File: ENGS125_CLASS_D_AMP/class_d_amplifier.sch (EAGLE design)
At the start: 24 parts, among them J1 BANANA_JACK_CT3151, J2 BANANA_JACK_CT3151, J3 BANANA_JACK_CT3151, J4 BANANA_JACK_CT3151, J5 BANANA_JACK_CT3151, J6 BANANA_JACK_CT3151, M1 BSC050NE2LSATMA1, M2 BSC050NE2LSATMA1, U1 LTC6992TSOT-23, U2 LTC4449

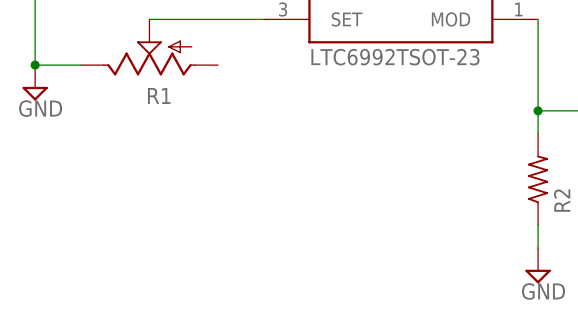
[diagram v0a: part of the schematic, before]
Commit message: Added Thayer shield to silkscreen on layout
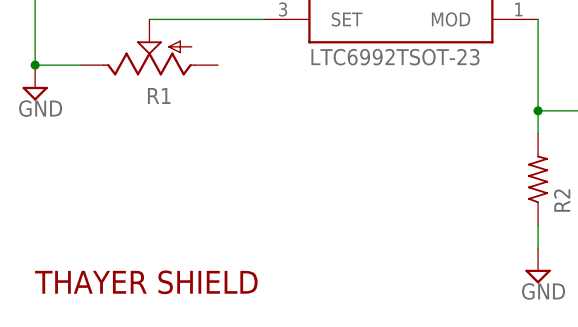
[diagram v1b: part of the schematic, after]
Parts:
- added U$1: THAYER, Engs125_lib_UPDATEFeb22_with_logo:THAYER
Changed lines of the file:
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@@
 <part name="J6" library="Engs125_lib_UPDATEFeb22" deviceset="BANANA_JACK_CT3151" device=""/>
 <part name="C8" library="Engs125_library" deviceset="C-US" device="" value="0.1u"/>
+<part name="U$1" library="Engs125_lib_UPDATEFeb22_with_logo" deviceset="THAYER" device=""/>
 </parts>
 <sheets>
@@
 <attribute name="VALUE" x="188.976" y="66.929" size="1.778" layer="96"/>
 </instance>
+<instance part="U$1" gate="G$1" x="-20.32" y="15.24" smashed="yes"/>
 </instances>
 <busses>

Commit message: Implemented edits from discussion with Stauth: GND pins, Gate pins, and extra input cap.
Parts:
- added C9: 1uF, Engs125_library:C-US
- added JP3, JP4, JP5, JP6, JP7: (no value), Engs125_lib_UPDATEFeb22:PINHD-1X1
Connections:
- net BG: now also JP4.1
- net GND: now also C9.2, JP5.1, JP6.1, JP7.1
- net TG: now also JP3.1
- net VIN: now also C9.1
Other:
- note added: "BG Probe"
- note added: "TG Probe"
- moved on the sheet: C5, C7

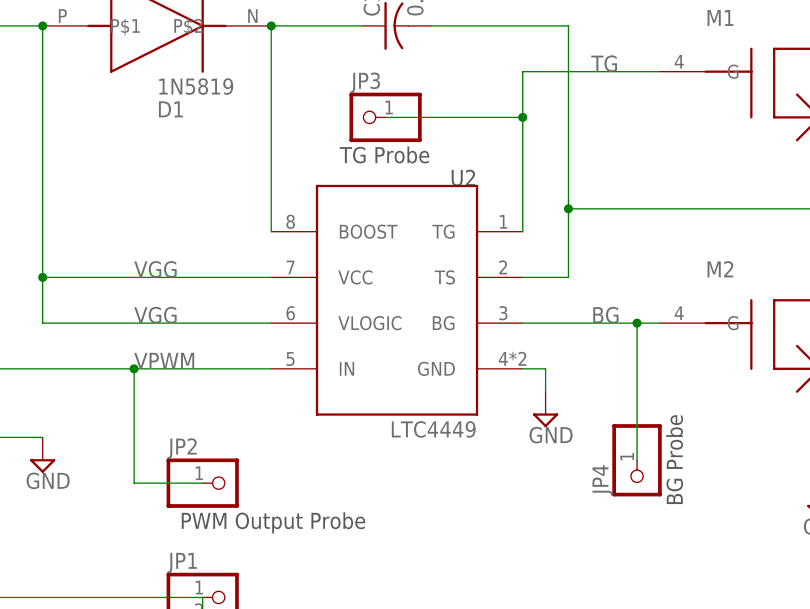
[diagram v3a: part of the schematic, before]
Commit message: Replaced gate driver IC with LTC4442
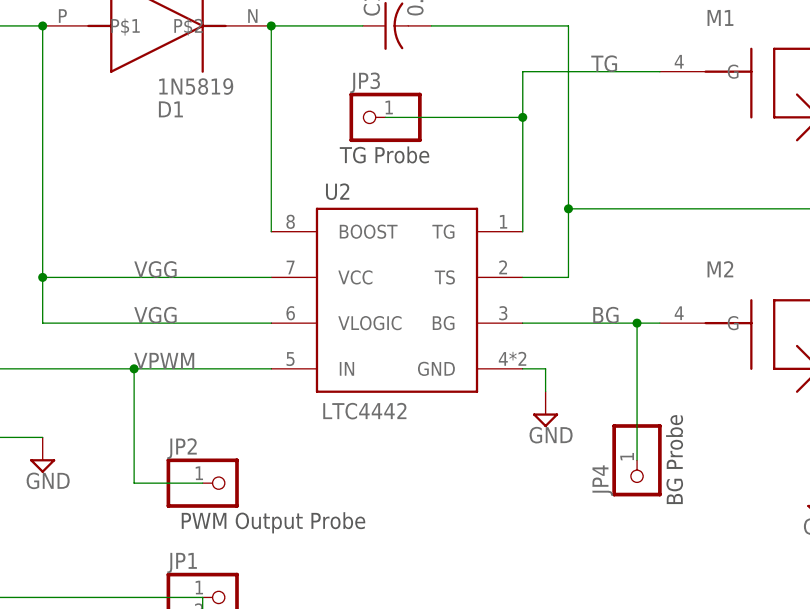
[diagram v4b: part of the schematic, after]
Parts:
- U2: value LTC4449 -> LTC4442; device Engs125_library:LTC4449 -> Engs125_lib_NEW_UPDATE_USE_THIS:LTC4442
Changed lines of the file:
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@@
 </classes>
 <parts>
-<part name="U2" library="Engs125_library" deviceset="LTC4449" device=""/>
+<part name="U2" library="Engs125_lib_NEW_UPDATE_USE_THIS" deviceset="LTC4442" device="" value="LTC4442"/>
 <part name="SUPPLY1" library="Engs125_library" deviceset="GND" device=""/>
 <part name="C3" library="Engs125_library" deviceset="C-US" device="" value="1uF"/>
@@
 </plain>
 <instances>
-<instance part="U2" gate="G$1" x="81.28" y="68.58" smashed="yes" rot="MR0">
-<attribute name="NAME" x="91.44" y="81.28" size="1.778" layer="97" rot="MR0"/>
-<attribute name="VALUE" x="91.44" y="53.34" size="1.778" layer="96" rot="MR0"/>
+<instance part="U2" gate="G$1" x="83.82" y="71.12" smashed="yes" rot="MR0">
+<attribute name="NAME" x="77.47" y="79.756" size="1.778" layer="97" rot="MR0"/>
+<attribute name="VALUE" x="83.82" y="55.372" size="1.778" layer="96" rot="MR0"/>
 </instance>
 <instance part="SUPPLY1" gate="GND" x="-20.32" y="38.1" smashed="yes">

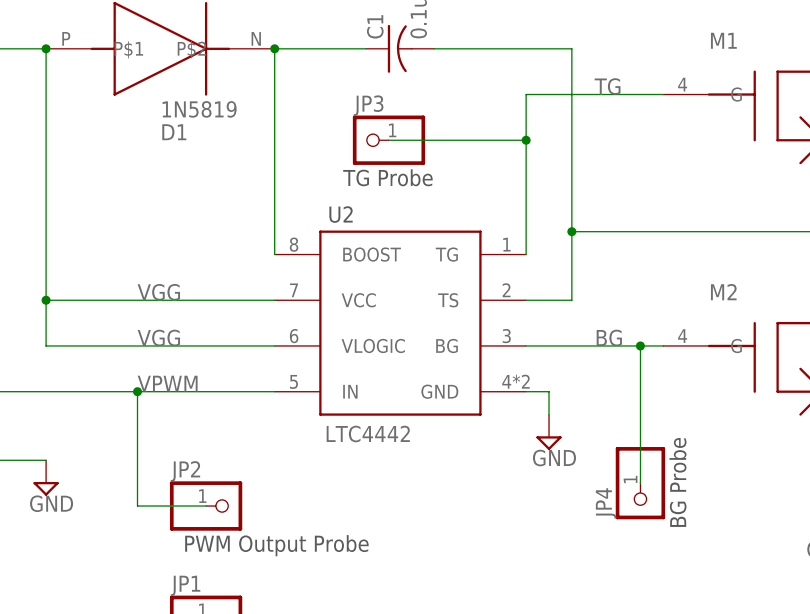
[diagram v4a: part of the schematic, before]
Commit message: Added converter specs to silkscreen
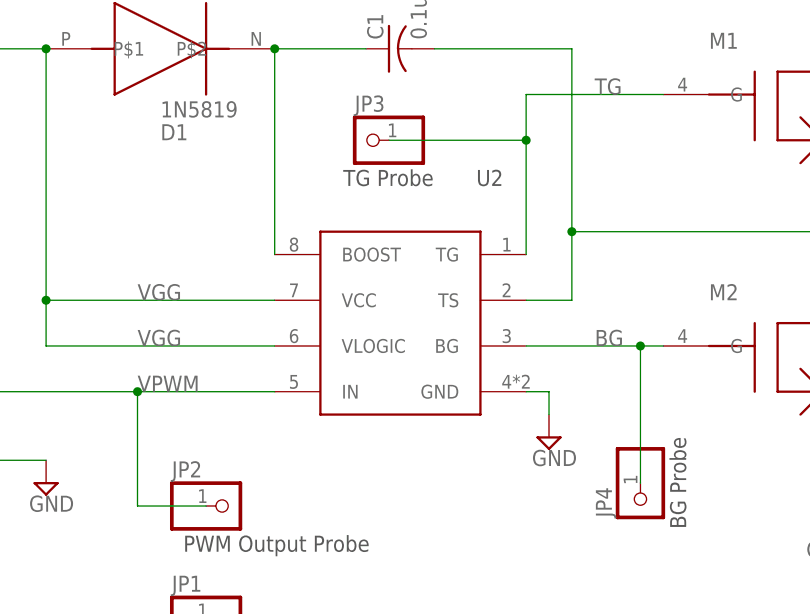
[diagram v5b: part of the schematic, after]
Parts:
- U2: value LTC4442 -> (none)
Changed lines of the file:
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@@
 </classes>
 <parts>
-<part name="U2" library="Engs125_lib_NEW_UPDATE_USE_THIS" deviceset="LTC4442" device="" value="LTC4442"/>
+<part name="U2" library="Engs125_lib_NEW_UPDATE_USE_THIS" deviceset="LTC4442" device=""/>
 <part name="SUPPLY1" library="Engs125_library" deviceset="GND" device=""/>
 <part name="C3" library="Engs125_library" deviceset="C-US" device="" value="1uF"/>
@@
 <instances>
 <instance part="U2" gate="G$1" x="83.82" y="71.12" smashed="yes" rot="MR0">
-<attribute name="NAME" x="77.47" y="79.756" size="1.778" layer="97" rot="MR0"/>
-<attribute name="VALUE" x="83.82" y="55.372" size="1.778" layer="96" rot="MR0"/>
+<attribute name="NAME" x="93.98" y="83.82" size="1.778" layer="97" rot="MR0"/>
+<attribute name="VALUE" x="93.98" y="55.88" size="1.778" layer="96" rot="MR0"/>
 </instance>
 <instance part="SUPPLY1" gate="GND" x="-20.32" y="38.1" smashed="yes">

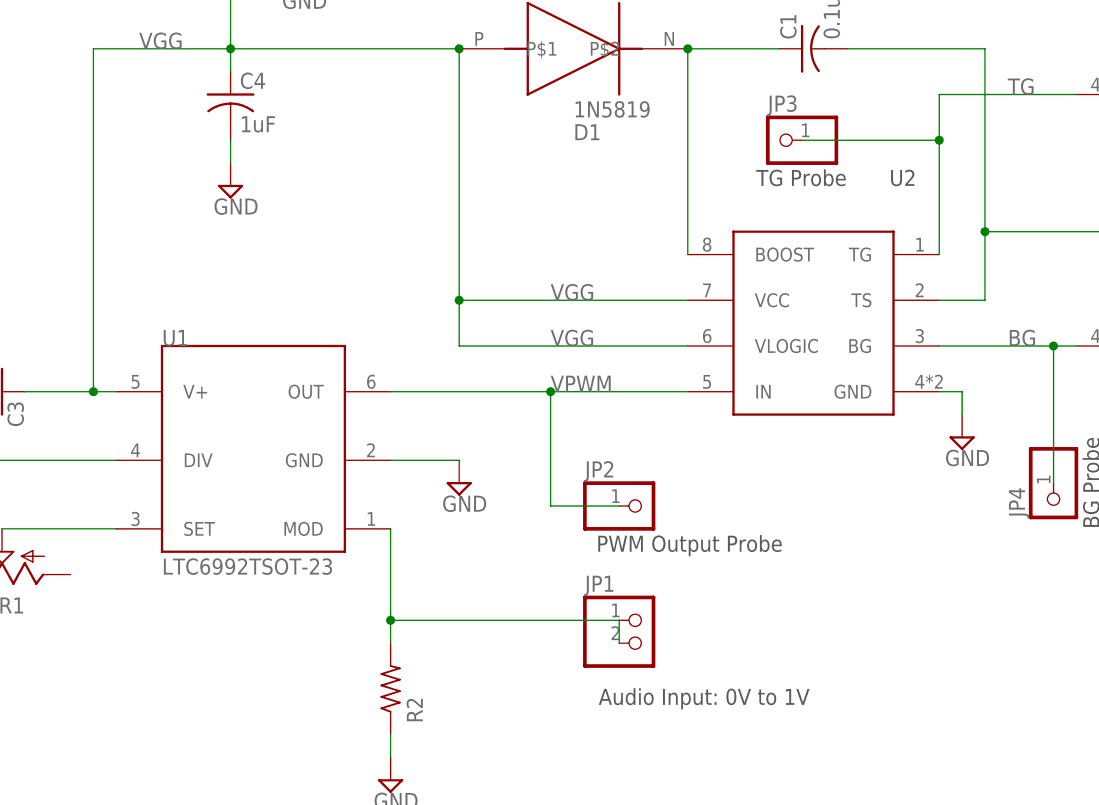
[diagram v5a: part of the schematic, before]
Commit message: Reorganized gate driver layout to account for fixed pin connections.
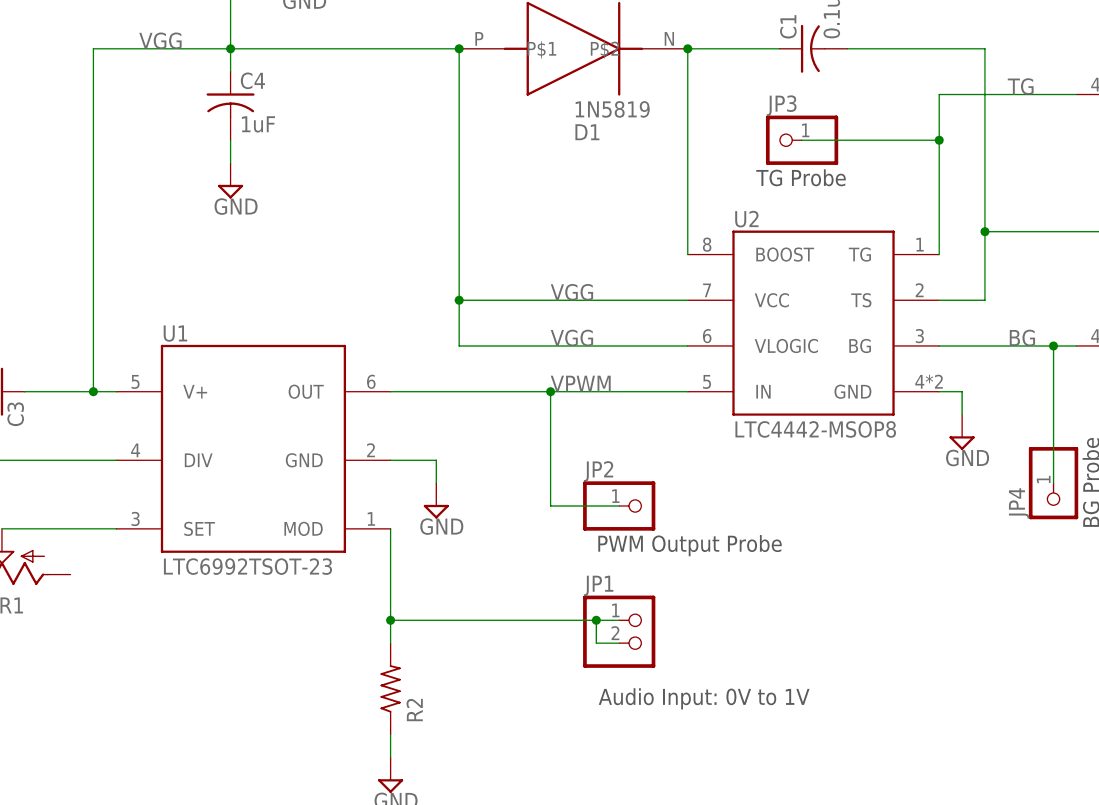
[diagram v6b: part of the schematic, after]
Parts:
- U2: value (none) -> LTC4442-MSOP8; device Engs125_lib_NEW_UPDATE_USE_THIS:LTC4442 -> Engs125_lib_NEW_UPDATE_USE_THIS_V2:LTC4442
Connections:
- net N$2 renamed BOOST
- removed net N$3: U1.GND
- net GND: now also U1.GND
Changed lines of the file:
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@@
 <setting verticaltext="up"/>
 </settings>
-<grid distance="0.1" unitdist="inch" unit="inch" style="lines" multiple="1" display="yes" altdistance="0.01" altunitdist="inch" altunit="inch"/>
+<grid distance="0.1" unitdist="inch" unit="inch" style="lines" multiple="1" display="no" altdistance="0.01" altunitdist="inch" altunit="inch"/>
 <layers>
 <layer number="1" name="Top" color="4" fill="1" visible="no" active="no"/>
@@
 </classes>
 <parts>
-<part name="U2" library="Engs125_lib_NEW_UPDATE_USE_THIS" deviceset="LTC4442" device=""/>
 <part name="SUPPLY1" library="Engs125_library" deviceset="GND" device=""/>
 <part name="C3" library="Engs125_library" deviceset="C-US" device="" value="1uF"/>
@@
 <part name="D1" library="Engs125_library" deviceset="DIODE" device="" value="1N5819"/>
 <part name="L1" library="Engs125_library" deviceset="SER2900" device="SER" value="33u"/>
-<part name="SUPPLY2" library="Engs125_library" deviceset="GND" device=""/>
 <part name="SUPPLY3" library="Engs125_library" deviceset="GND" device=""/>
 <part name="SUPPLY4" library="Engs125_library" deviceset="GND" device=""/>
@@
 <part name="SUPPLY11" library="Engs125_library" deviceset="GND" device=""/>
 <part name="C9" library="Engs125_library" deviceset="C-US" device="" value="1uF"/>
+<part name="SUPPLY2" library="Engs125_library" deviceset="GND" device=""/>
+<part name="U2" library="Engs125_lib_NEW_UPDATE_USE_THIS_V2" deviceset="LTC4442" device="" value="LTC4442-MSOP8"/>
 </parts>
 <sheets>
@@
 </plain>
 <instances>
-<instance part="U2" gate="G$1" x="83.82" y="71.12" smashed="yes" rot="MR0">
-<attribute name="NAME" x="93.98" y="83.82" size="1.778" layer="97" rot="MR0"/>
-<attribute name="VALUE" x="93.98" y="55.88" size="1.778" layer="96" rot="MR0"/>
-</instance>
 <instance part="SUPPLY1" gate="GND" x="-20.32" y="38.1" smashed="yes">
 <attribute name="VALUE" x="-22.225" y="34.925" size="1.778" layer="96"/>
@@
 <attribute name="NAME" x="147.32" y="82.296" size="1.27" layer="95"/>
 </instance>
-<instance part="SUPPLY2" gate="GND" x="43.18" y="50.8" smashed="yes">
-<attribute name="VALUE" x="41.275" y="47.625" size="1.778" layer="96"/>
-</instance>
 <instance part="SUPPLY3" gate="GND" x="35.56" y="17.78" smashed="yes">
 <attribute name="VALUE" x="33.655" y="14.605" size="1.778" layer="96"/>
@@
 </instance>
 <instance part="U1" gate="G$1" x="20.32" y="53.34" smashed="yes">
-<attribute name="NAME" x="10.16" y="66.04" size="1.778" layer="95"/>
+<attribute name="NAME" x="10.16" y="66.548" size="1.778" layer="95"/>
 <attribute name="VALUE" x="10.16" y="40.64" size="1.778" layer="96"/>
 </instance>
@@
 <attribute name="NAME" x="120.396" y="122.555" size="1.778" layer="95"/>
 <attribute name="VALUE" x="120.396" y="117.729" size="1.778" layer="96"/>
+</instance>
+<instance part="SUPPLY2" gate="GND" x="40.64" y="48.26" smashed="yes">
+<attribute name="VALUE" x="38.735" y="45.085" size="1.778" layer="96"/>
+</instance>
+<instance part="U2" gate="G$1" x="81.28" y="71.12" smashed="yes">
+<attribute name="NAME" x="73.66" y="79.248" size="1.778" layer="95"/>
+<attribute name="VALUE" x="73.66" y="55.88" size="1.778" layer="96"/>
 </instance>
 </instances>
@@
 <pinref part="SUPPLY10" gate="GND" pin="GND"/>
 <wire x1="99.06" y1="58.42" x2="99.06" y2="60.96" width="0.1524" layer="91"/>
+<wire x1="99.06" y1="60.96" x2="96.52" y2="60.96" width="0.1524" layer="91"/>
 <pinref part="U2" gate="G$1" pin="GND"/>
-<wire x1="99.06" y1="60.96" x2="96.52" y2="60.96" width="0.1524" layer="91"/>
 </segment>
 <segment>
@@
 <wire x1="205.74" y1="132.08" x2="195.58" y2="132.08" width="0.1524" layer="91"/>
 <wire x1="205.74" y1="139.7" x2="205.74" y2="132.08" width="0.1524" layer="91"/>
+</segment>
+<segment>
+<pinref part="U1" gate="G$1" pin="GND"/>
+<wire x1="35.56" y1="53.34" x2="40.64" y2="53.34" width="0.1524" layer="91"/>
+<wire x1="40.64" y1="53.34" x2="40.64" y2="50.8" width="0.1524" layer="91"/>
+<pinref part="SUPPLY2" gate="GND" pin="GND"/>
 </segment>
 </net>
@@
 <wire x1="43.18" y1="99.06" x2="43.18" y2="71.12" width="0.1524" layer="91"/>
 <junction x="43.18" y="99.06"/>
-<pinref part="U2" gate="G$1" pin="VCC"/>
 <wire x1="43.18" y1="71.12" x2="68.58" y2="71.12" width="0.1524" layer="91"/>
-<pinref part="U2" gate="G$1" pin="VLOGIC"/>
 <wire x1="43.18" y1="71.12" x2="43.18" y2="66.04" width="0.1524" layer="91"/>
 <wire x1="43.18" y1="66.04" x2="68.58" y2="66.04" width="0.1524" layer="91"/>
@@
 <pinref part="J1" gate="G$1" pin="IN"/>
 <pinref part="U1" gate="G$1" pin="V+"/>
+<pinref part="U2" gate="G$1" pin="VCC"/>
+<pinref part="U2" gate="G$1" pin="VLOGIC"/>
 </segment>
 </net>
 <net name="VPWM" class="0">
 <segment>
-<pinref part="U2" gate="G$1" pin="IN"/>
 <wire x1="35.56" y1="60.96" x2="53.34" y2="60.96" width="0.1524" layer="91"/>
 <label x="53.34" y="60.96" size="1.778" layer="95"/>
@@
 <wire x1="53.34" y1="48.26" x2="60.96" y2="48.26" width="0.1524" layer="91"/>
 <junction x="53.34" y="60.96"/>
-</segment>
-</net>
-<net name="N$2" class="0">
+<pinref part="U2" gate="G$1" pin="IN"/>
+</segment>
+</net>
+<net name="BOOST" class="0">
 <segment>
 <pinref part="D1" gate="G$1" pin="P$2"/>
-<pinref part="U2" gate="G$1" pin="BOOST"/>
 <wire x1="68.58" y1="99.06" x2="68.58" y2="76.2" width="0.1524" layer="91"/>
 <pinref part="C1" gate="G$1" pin="1"/>
 <wire x1="68.58" y1="99.06" x2="78.74" y2="99.06" width="0.1524" layer="91"/>
 <junction x="68.58" y="99.06"/>
+<pinref part="U2" gate="G$1" pin="BOOST"/>
 </segment>
 </net>
@@
 <pinref part="C1" gate="G$1" pin="2"/>
 <wire x1="86.36" y1="99.06" x2="101.6" y2="99.06" width="0.1524" layer="91"/>
-<pinref part="U2" gate="G$1" pin="TS"/>
 <wire x1="101.6" y1="99.06" x2="101.6" y2="78.74" width="0.1524" layer="91"/>
 <wire x1="101.6" y1="78.74" x2="101.6" y2="71.12" width="0.1524" layer="91"/>
@@
 <wire x1="137.16" y1="76.2" x2="139.7" y2="76.2" width="0.1524" layer="91"/>
 <junction x="137.16" y="76.2"/>
+<pinref part="U2" gate="G$1" pin="TS"/>
 </segment>
 </net>
@@
 <net name="BG" class="0">
 <segment>
-<pinref part="U2" gate="G$1" pin="BG"/>
 <label x="104.14" y="66.04" size="1.778" layer="95"/>
 <pinref part="M2" gate="G$1" pin="G"/>
@@
 <wire x1="109.22" y1="50.8" x2="109.22" y2="66.04" width="0.1524" layer="91"/>
 <junction x="109.22" y="66.04"/>
+<pinref part="U2" gate="G$1" pin="BG"/>
 </segment>
 </net>
 <net name="TG" class="0">
 <segment>
-<pinref part="U2" gate="G$1" pin="TG"/>
 <wire x1="96.52" y1="76.2" x2="96.52" y2="88.9" width="0.1524" layer="91"/>
 <wire x1="96.52" y1="88.9" x2="96.52" y2="93.98" width="0.1524" layer="91"/>
@@
 <wire x1="81.28" y1="88.9" x2="96.52" y2="88.9" width="0.1524" layer="91"/>
 <junction x="96.52" y="88.9"/>
-</segment>
-</net>
-<net name="N$3" class="0">
-<segment>
-<pinref part="SUPPLY2" gate="GND" pin="GND"/>
-<wire x1="43.18" y1="53.34" x2="35.56" y2="53.34" width="0.1524" layer="91"/>
-<pinref part="U1" gate="G$1" pin="GND"/>
+<pinref part="U2" gate="G$1" pin="TG"/>
 </segment>
 </net>
@@
 <net name="N$4" class="0">
 <segment>
-<pinref part="JP1" gate="G$1" pin="2"/>
 <pinref part="JP1" gate="G$1" pin="1"/>
-<wire x1="60.96" y1="35.56" x2="60.96" y2="33.02" width="0.1524" layer="91"/>
 <pinref part="R2" gate="G$1" pin="2"/>
 <pinref part="U1" gate="G$1" pin="MOD"/>
 <wire x1="35.56" y1="45.72" x2="35.56" y2="35.56" width="0.1524" layer="91"/>
 <wire x1="35.56" y1="35.56" x2="35.56" y2="33.02" width="0.1524" layer="91"/>
-<wire x1="60.96" y1="35.56" x2="35.56" y2="35.56" width="0.1524" layer="91"/>
+<wire x1="60.96" y1="35.56" x2="58.42" y2="35.56" width="0.1524" layer="91"/>
 <junction x="35.56" y="35.56"/>
-</segment>
-</net>
+<pinref part="JP1" gate="G$1" pin="2"/>
+<wire x1="58.42" y1="35.56" x2="35.56" y2="35.56" width="0.1524" layer="91"/>
+<wire x1="60.96" y1="33.02" x2="58.42" y2="33.02" width="0.1524" layer="91"/>
+<wire x1="58.42" y1="33.02" x2="58.42" y2="35.56" width="0.1524" layer="91"/>
+<junction x="58.42" y="35.56"/>
+</segment>
+</net>
